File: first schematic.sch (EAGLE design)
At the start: 13 parts, among them IC1 ATMEGA328P, U1 ADXL362

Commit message: Add files via upload
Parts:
- removed B1: 3V, One_Dimensional_Pong:BATTERYCR2540-SMT
- removed RESETSW: (no value), adafruit:SWITCH_PUSHBUTTONC&K_KSS
- added S1: EVP-BFAC1A000, EVP-BFAC1A000:EVP-BFAC1A000
- added U$1, U$2, U$3: FIDUCIAL, adafruit:FIDUCIAL
- added U$4: CR2032, cr2032:CR2032
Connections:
- net GRND: now also S1.A', U$4.GRND; no longer B1.-, RESETSW.P$1
- net N$7: now also S1.A; no longer RESETSW.P$2
- net VCC: now also U$4.VCC; no longer B1.+
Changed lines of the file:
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@@
 <?xml version="1.0" encoding="utf-8"?>
 <!DOCTYPE eagle SYSTEM "eagle.dtd">
-<eagle version="9.5.1">
+<eagle version="9.6.2">
 <drawing>
 <settings>
@@
 </classes>
 <parts>
-<part name="B1" library="One_Dimensional_Pong" library_urn="urn:adsk.eagle:library:15955360" deviceset="BATTERY" device="CR2540-SMT" package3d_urn="urn:adsk.eagle:package:15955390/5" value="3V"/>
 <part name="C1" library="adafruit" library_urn="urn:adsk.eagle:library:420" deviceset="C-US" device="C0805" package3d_urn="urn:adsk.eagle:package:6240337/1" value="100nF"/>
 <part name="XTAL" library="adafruit" library_urn="urn:adsk.eagle:library:420" deviceset="CRYSTAL" device="HC49UP" package3d_urn="urn:adsk.eagle:package:6240908/1" value="16MHz"/>
 <part name="C2" library="adafruit" library_urn="urn:adsk.eagle:library:420" deviceset="C-US" device="C0805" package3d_urn="urn:adsk.eagle:package:6240337/1" value="100nF"/>
 <part name="R1" library="adafruit" library_urn="urn:adsk.eagle:library:420" deviceset="R-US_" device="R0805" package3d_urn="urn:adsk.eagle:package:6240566/1" value="10K"/>
-<part name="RESETSW" library="adafruit" library_urn="urn:adsk.eagle:library:420" deviceset="SWITCH_PUSHBUTTON" device="C&amp;K_KSS" package3d_urn="urn:adsk.eagle:package:6240958/1"/>
 <part name="JP1" library="Connector" library_urn="urn:adsk.eagle:library:16378166" deviceset="PINHD-2X3" device="" package3d_urn="urn:adsk.eagle:package:22462/2"/>
 <part name="IC1" library="IC_Embedded" library_urn="urn:adsk.eagle:library:16378270" deviceset="ATMEGA328PB" device="_TQFP" package3d_urn="urn:adsk.eagle:package:16494913/1" value="ATMEGA328P"/>
@@
 <part name="C5" library="adafruit" library_urn="urn:adsk.eagle:library:420" deviceset="C-US" device="C0805" package3d_urn="urn:adsk.eagle:package:6240337/1" value="1uF"/>
 <part name="U1" library="ADXL362" deviceset="ADXL362" device=""/>
+<part name="S1" library="EVP-BFAC1A000" deviceset="EVP-BFAC1A000" device=""/>
+<part name="U$4" library="cr2032" deviceset="CR2032" device=""/>
+<part name="U$1" library="adafruit" library_urn="urn:adsk.eagle:library:420" deviceset="FIDUCIAL" device="" package3d_urn="urn:adsk.eagle:package:6240632/1"/>
+<part name="U$2" library="adafruit" library_urn="urn:adsk.eagle:library:420" deviceset="FIDUCIAL" device="" package3d_urn="urn:adsk.eagle:package:6240632/1"/>
+<part name="U$3" library="adafruit" library_urn="urn:adsk.eagle:library:420" deviceset="FIDUCIAL" device="" package3d_urn="urn:adsk.eagle:package:6240632/1"/>
 </parts>
 <sheets>
@@
 </plain>
 <instances>
-<instance part="B1" gate="G$1" x="63.5" y="86.36" smashed="yes" rot="R90">
-<attribute name="NAME" x="60.325" y="83.82" size="1.27" layer="95" rot="R90"/>
-<attribute name="VALUE" x="68.58" y="83.82" size="1.27" layer="96" rot="R90"/>
-</instance>
 <instance part="C1" gate="G$1" x="83.82" y="119.38" smashed="yes">
 <attribute name="NAME" x="84.836" y="120.015" size="1.778" layer="95"/>
@@
 <attribute name="VALUE" x="100.33" y="132.842" size="1.778" layer="96" rot="R180"/>
 </instance>
-<instance part="RESETSW" gate="G$1" x="88.9" y="132.08" smashed="yes">
-<attribute name="NAME" x="86.36" y="135.636" size="1.27" layer="95"/>
-<attribute name="VALUE" x="86.36" y="129.794" size="1.27" layer="96"/>
-</instance>
 <instance part="JP1" gate="A" x="256.54" y="81.28" smashed="yes" rot="R90">
 <attribute name="NAME" x="250.825" y="74.93" size="1.778" layer="95" rot="R90"/>
@@
 <attribute name="VALUE" x="63.5" y="157.988" size="1.778" layer="96" ratio="12"/>
 </instance>
+<instance part="S1" gate="G$1" x="86.36" y="139.7" smashed="yes">
+<attribute name="NAME" x="87.63" y="142.24" size="1.778" layer="95" align="center-left"/>
+<attribute name="VALUE" x="87.63" y="129.54" size="1.778" layer="96" align="center-left"/>
+</instance>
+<instance part="U$4" gate="G$1" x="63.5" y="86.36" smashed="yes"/>
+<instance part="U$1" gate="G$1" x="45.72" y="187.96" smashed="yes"/>
+<instance part="U$2" gate="G$1" x="45.72" y="55.88" smashed="yes"/>
+<instance part="U$3" gate="G$1" x="276.86" y="55.88" smashed="yes"/>
 </instances>
 <busses>
@@
 <wire x1="81.28" y1="124.46" x2="91.44" y2="124.46" width="0.1524" layer="91"/>
 <junction x="81.28" y="124.46"/>
-<pinref part="B1" gate="G$1" pin="+"/>
 <wire x1="63.5" y1="124.46" x2="76.2" y2="124.46" width="0.1524" layer="91"/>
 <wire x1="76.2" y1="124.46" x2="78.74" y2="124.46" width="0.1524" layer="91"/>
 <wire x1="78.74" y1="124.46" x2="81.28" y2="124.46" width="0.1524" layer="91"/>
-<wire x1="63.5" y1="88.9" x2="63.5" y2="93.98" width="0.1524" layer="91"/>
 <pinref part="IC1" gate="G$1" pin="AVCC"/>
-<wire x1="63.5" y1="93.98" x2="63.5" y2="124.46" width="0.1524" layer="91"/>
+<wire x1="63.5" y1="93.98" x2="63.5" y2="96.52" width="0.1524" layer="91"/>
+<wire x1="63.5" y1="96.52" x2="63.5" y2="124.46" width="0.1524" layer="91"/>
 <wire x1="205.74" y1="93.98" x2="215.9" y2="93.98" width="0.1524" layer="91"/>
 <wire x1="215.9" y1="93.98" x2="220.98" y2="93.98" width="0.1524" layer="91"/>
@@
 <wire x1="53.34" y1="58.42" x2="53.34" y2="93.98" width="0.1524" layer="91"/>
 <wire x1="53.34" y1="93.98" x2="63.5" y2="93.98" width="0.1524" layer="91"/>
-<junction x="63.5" y="93.98"/>
 <pinref part="IC1" gate="G$1" pin="VCC"/>
 <wire x1="205.74" y1="88.9" x2="205.74" y2="93.98" width="0.1524" layer="91"/>
@@
 <wire x1="78.74" y1="177.8" x2="78.74" y2="124.46" width="0.1524" layer="91"/>
 <junction x="78.74" y="124.46"/>
+<pinref part="U$4" gate="G$1" pin="VCC"/>
+<junction x="63.5" y="96.52"/>
 </segment>
 </net>
 <net name="GRND" class="0">
 <segment>
-<pinref part="B1" gate="G$1" pin="-"/>
 <wire x1="63.5" y1="83.82" x2="71.12" y2="83.82" width="0.1524" layer="91"/>
 <wire x1="71.12" y1="83.82" x2="71.12" y2="114.3" width="0.1524" layer="91"/>
 <wire x1="71.12" y1="114.3" x2="71.12" y2="132.08" width="0.1524" layer="91"/>
 <label x="73.66" y="99.06" size="1.778" layer="95"/>
-<pinref part="RESETSW" gate="G$1" pin="P$1"/>
-<wire x1="83.82" y1="132.08" x2="76.2" y2="132.08" width="0.1524" layer="91"/>
+<wire x1="81.28" y1="132.08" x2="76.2" y2="132.08" width="0.1524" layer="91"/>
 <pinref part="C1" gate="G$1" pin="2"/>
 <pinref part="C2" gate="G$1" pin="2"/>
@@
 <wire x1="205.74" y1="63.5" x2="63.5" y2="63.5" width="0.1524" layer="91"/>
 <wire x1="63.5" y1="63.5" x2="63.5" y2="83.82" width="0.1524" layer="91"/>
-<junction x="63.5" y="83.82"/>
 <pinref part="C4" gate="G$1" pin="2"/>
 <wire x1="99.06" y1="109.22" x2="99.06" y2="114.3" width="0.1524" layer="91"/>
@@
 <junction x="76.2" y="132.08"/>
 <junction x="205.74" y="63.5"/>
+<pinref part="S1" gate="G$1" pin="A'"/>
+<wire x1="81.28" y1="132.08" x2="81.28" y2="134.62" width="0.1524" layer="91"/>
+<pinref part="U$4" gate="G$1" pin="GRND"/>
+<junction x="63.5" y="83.82"/>
 </segment>
 </net>
@@
 <pinref part="R1" gate="G$1" pin="1"/>
 <wire x1="101.6" y1="129.54" x2="101.6" y2="132.08" width="0.1524" layer="91"/>
-<pinref part="RESETSW" gate="G$1" pin="P$2"/>
-<wire x1="101.6" y1="132.08" x2="93.98" y2="132.08" width="0.1524" layer="91"/>
 <wire x1="101.6" y1="132.08" x2="114.3" y2="132.08" width="0.1524" layer="91"/>
-<junction x="101.6" y="132.08"/>
 <wire x1="114.3" y1="132.08" x2="114.3" y2="83.82" width="0.1524" layer="91"/>
 <pinref part="IC1" gate="G$1" pin="PC6(!RESET)"/>
@@
 <wire x1="121.92" y1="68.58" x2="121.92" y2="83.82" width="0.1524" layer="91"/>
 <junction x="121.92" y="83.82"/>
+<pinref part="S1" gate="G$1" pin="A"/>
+<wire x1="99.06" y1="134.62" x2="101.6" y2="134.62" width="0.1524" layer="91"/>
+<wire x1="101.6" y1="134.62" x2="101.6" y2="132.08" width="0.1524" layer="91"/>
+<junction x="101.6" y="132.08"/>
 </segment>
 </net>

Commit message: Rev2
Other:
- note added: "11/27/2020"
- note added: "3.0"
- note added: "388 Pedometer"
- note added: "N/A"
- moved on the sheet: C1, C2, C3, C4, C5, IC1, J1, JP1, R1, S1, U1, XTAL

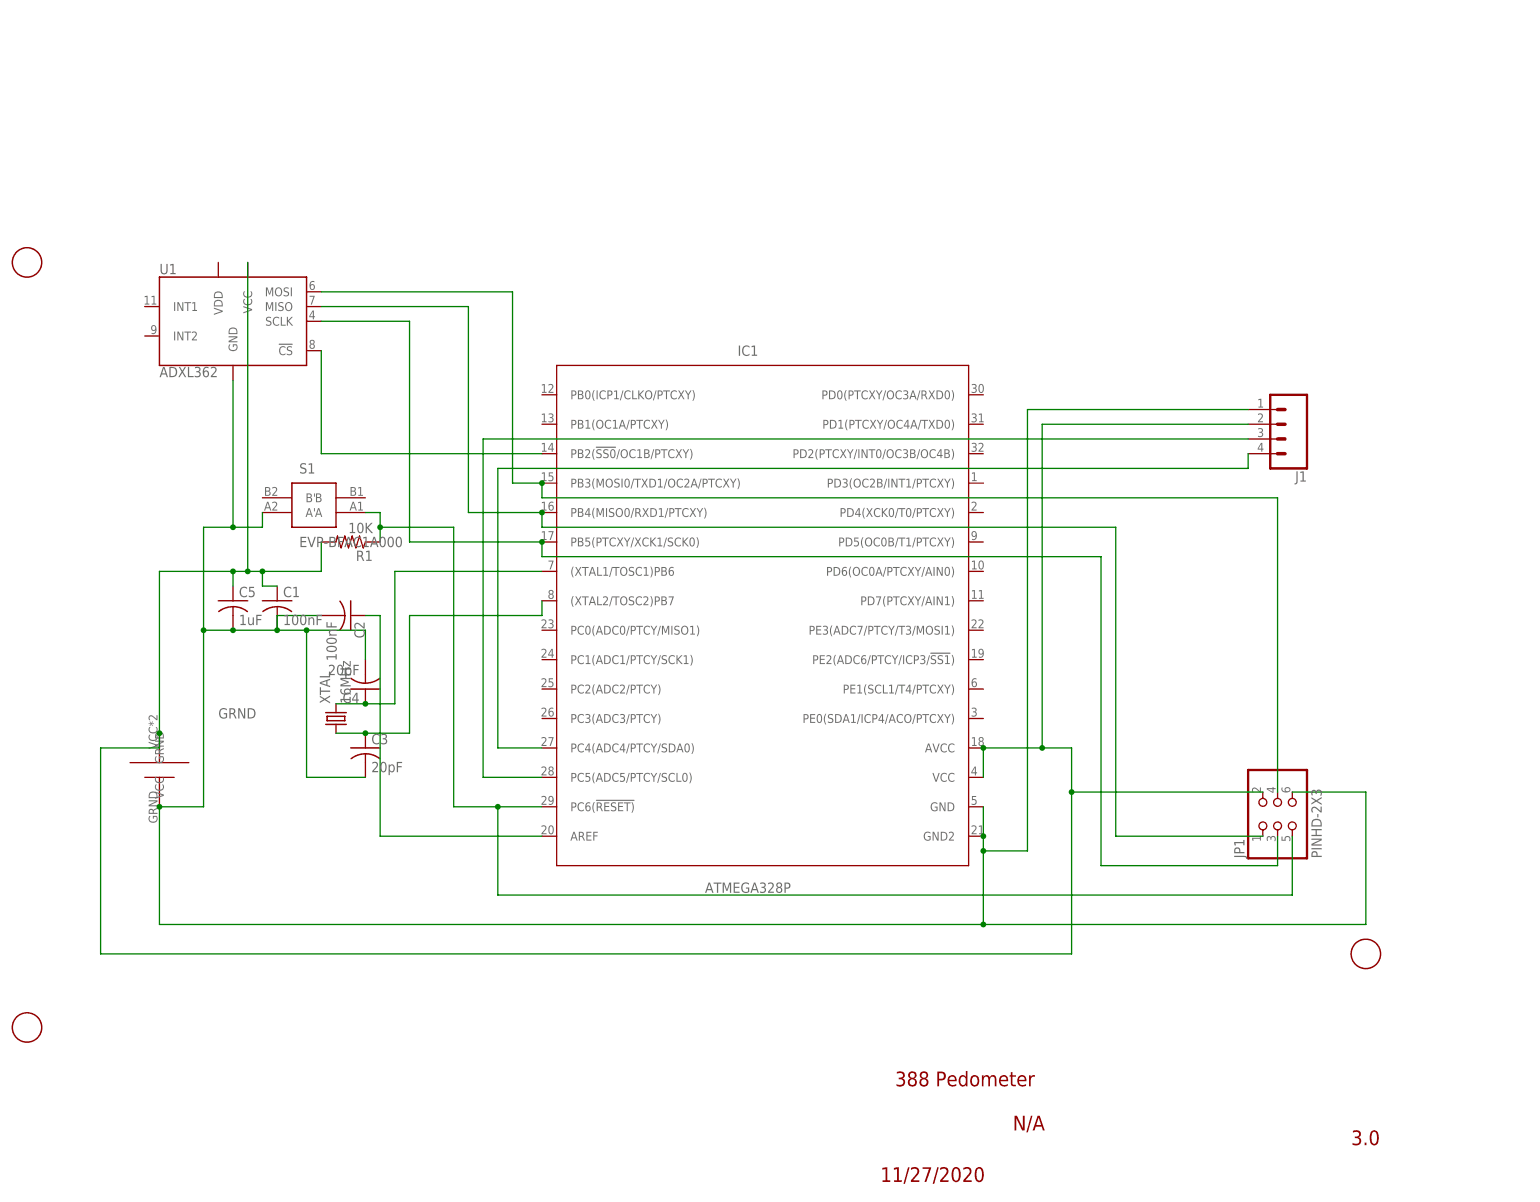
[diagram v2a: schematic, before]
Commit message: fixed issues with schematic
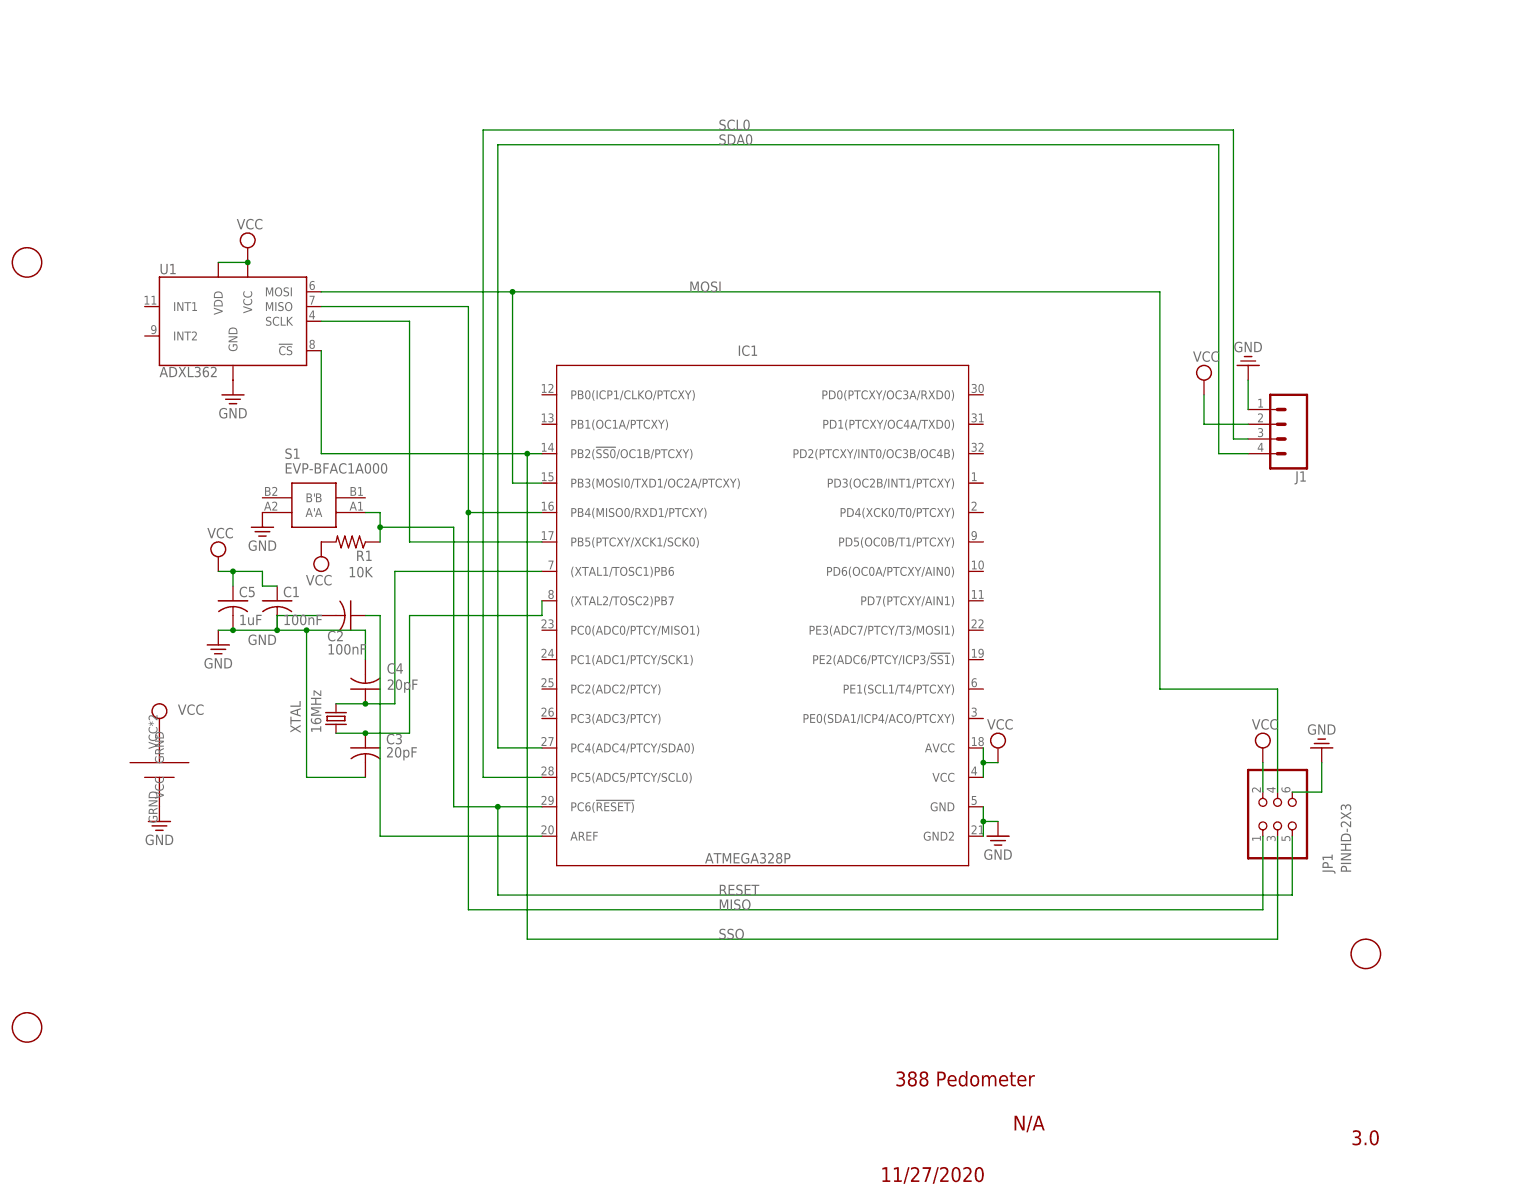
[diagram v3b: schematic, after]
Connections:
- net GRND renamed GND
- net N$10 renamed SDA0
- net N$3 renamed MOSI
- net N$5 renamed MISO
- net N$7 renamed RESET
- net N$9 renamed SCL0
- removed net N$14: IC1.PB2(!SS0!/OC1B/PTCXY), U1.!CS
- removed net N$6: IC1.PB5(PTCXY/XCK1/SCK0), JP1.3, U1.SCLK
- new net N$9: IC1.PB5(PTCXY/XCK1/SCK0), U1.SCLK
- new net SSO: IC1.PB2(!SS0!/OC1B/PTCXY), JP1.3, U1.!CS
- net VCC: now also U1.VDD

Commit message: final update
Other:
- moved on the sheet: C2
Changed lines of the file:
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@@
 <part name="SUPPLY13" library="Fidget Spinner Example" library_urn="urn:adsk.eagle:library:9489508" deviceset="VCC" device=""/>
 <part name="SUPPLY14" library="Fidget Spinner Example" library_urn="urn:adsk.eagle:library:9489508" deviceset="VCC" device=""/>
+<part name="SUPPLY15" library="Power_Symbols" library_urn="urn:adsk.eagle:library:16502351" deviceset="GND-EARTH" device="" value="GND"/>
 </parts>
 <sheets>
@@
 <attribute name="VALUE" x="71.12" y="66.04" size="1.778" layer="96" rot="R90"/>
 </instance>
-<instance part="C2" gate="G$1" x="76.2" y="86.36" smashed="yes" rot="R270">
-<attribute name="NAME" x="72.136" y="81.915" size="1.778" layer="95"/>
-<attribute name="VALUE" x="72.136" y="79.629" size="1.778" layer="96"/>
+<instance part="C2" gate="G$1" x="91.44" y="48.26" smashed="yes" rot="R270">
+<attribute name="NAME" x="87.376" y="43.815" size="1.778" layer="95"/>
+<attribute name="VALUE" x="87.376" y="41.529" size="1.778" layer="96"/>
 </instance>
 <instance part="R1" gate="G$1" x="76.2" y="99.06" smashed="yes" rot="R180">
@@
 <attribute name="VALUE" x="187.96" y="45.085" size="1.778" layer="96" align="center"/>
 </instance>
-<instance part="SUPPLY7" gate="G$1" x="231.14" y="129.54" smashed="yes" rot="R180">
-<attribute name="VALUE" x="231.14" y="132.715" size="1.778" layer="96" rot="R180" align="center"/>
+<instance part="SUPPLY7" gate="G$1" x="236.22" y="129.54" smashed="yes">
+<attribute name="VALUE" x="236.22" y="126.365" size="1.778" layer="96" align="center"/>
 </instance>
-<instance part="SUPPLY8" gate="G$1" x="243.84" y="63.5" smashed="yes" rot="R180">
-<attribute name="VALUE" x="243.84" y="66.675" size="1.778" layer="96" rot="R180" align="center"/>
+<instance part="SUPPLY8" gate="G$1" x="243.84" y="53.34" smashed="yes">
+<attribute name="VALUE" x="243.84" y="50.165" size="1.778" layer="96" align="center"/>
 </instance>
 <instance part="SUPPLY9" gate="G$1" x="53.34" y="81.28" smashed="yes">
@@
 <instance part="SUPPLY14" gate="G$1" x="58.42" y="149.86" smashed="yes">
 <attribute name="VALUE" x="56.515" y="153.035" size="1.778" layer="96"/>
+</instance>
+<instance part="SUPPLY15" gate="G$1" x="83.82" y="45.72" smashed="yes">
+<attribute name="VALUE" x="83.82" y="42.545" size="1.778" layer="96" align="center"/>
 </instance>
 </instances>
@@
 </segment>
 <segment>
-<pinref part="SUPPLY7" gate="G$1" pin="GND"/>
-<pinref part="J1" gate="G$1" pin="1"/>
-<wire x1="231.14" y1="127" x2="231.14" y2="121.92" width="0.1524" layer="91"/>
-</segment>
-<segment>
 <pinref part="JP1" gate="A" pin="6"/>
 <pinref part="SUPPLY8" gate="G$1" pin="GND"/>
 <wire x1="238.76" y1="55.88" x2="243.84" y2="55.88" width="0.1524" layer="91"/>
-<wire x1="243.84" y1="55.88" x2="243.84" y2="60.96" width="0.1524" layer="91"/>
 </segment>
 <segment>
 <label x="58.42" y="81.28" size="1.778" layer="95"/>
 <pinref part="C1" gate="G$1" pin="2"/>
-<pinref part="C2" gate="G$1" pin="2"/>
-<wire x1="71.12" y1="86.36" x2="63.5" y2="86.36" width="0.1524" layer="91"/>
 <wire x1="63.5" y1="86.36" x2="63.5" y2="83.82" width="0.1524" layer="91"/>
 <wire x1="63.5" y1="83.82" x2="55.88" y2="83.82" width="0.1524" layer="91"/>
@@
 <pinref part="SUPPLY11" gate="G$1" pin="GND"/>
 </segment>
+<segment>
+<pinref part="J1" gate="G$1" pin="1"/>
+<pinref part="SUPPLY7" gate="G$1" pin="GND"/>
+<wire x1="231.14" y1="121.92" x2="231.14" y2="132.08" width="0.1524" layer="91"/>
+<wire x1="231.14" y1="132.08" x2="236.22" y2="132.08" width="0.1524" layer="91"/>
+</segment>
+<segment>
+<pinref part="SUPPLY15" gate="G$1" pin="GND"/>
+<pinref part="C2" gate="G$1" pin="2"/>
+<wire x1="83.82" y1="48.26" x2="86.36" y2="48.26" width="0.1524" layer="91"/>
+</segment>
 </net>
 <net name="AREFTOCAP" class="0">
 <segment>
+<pinref part="IC1" gate="G$1" pin="AREF"/>
+<wire x1="109.22" y1="48.26" x2="93.98" y2="48.26" width="0.1524" layer="91"/>
 <pinref part="C2" gate="G$1" pin="1"/>
-<wire x1="81.28" y1="86.36" x2="78.74" y2="86.36" width="0.1524" layer="91"/>
-<pinref part="IC1" gate="G$1" pin="AREF"/>
-<wire x1="109.22" y1="48.26" x2="81.28" y2="48.26" width="0.1524" layer="91"/>
-<wire x1="81.28" y1="48.26" x2="81.28" y2="86.36" width="0.1524" layer="91"/>
 </segment>
 </net>
